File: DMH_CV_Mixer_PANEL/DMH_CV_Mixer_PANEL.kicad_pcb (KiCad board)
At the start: 2 copper layers, 50 x 200 mm, 25 parts, among them J0 Panel_GND_Solder_Wire_Pad

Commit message: Panel design done
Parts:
- H10: value CV C Amt -> In C2
- H12: value Offset B -> In B1; footprint SynthStuff:Pot_Cutout_Tiny -> SynthStuff:Pot_Cutout_Tiny_attv_P110KH1
- H13: value CV B Amt -> In B2
- H14: value In C -> In C1
- H15: value In B -> In B1
- H17: value CV B -> In B2
- H18: value CV C -> In C2
- H19: value Offset D -> In D1; footprint SynthStuff:Pot_Cutout_Tiny -> SynthStuff:Pot_Cutout_Tiny_attv_P110KH1
- H20: value CV D Amt -> In D2
- H21: value In D -> In D1
- H22: value CV D -> In D2
- H5: value Offset A -> In A1; footprint SynthStuff:Pot_Cutout_Tiny -> SynthStuff:Pot_Cutout_Tiny_attv_P110KH1
- H6: value CV A Amt -> In A2
- H7: value Offset C -> In C1; footprint SynthStuff:Pot_Cutout_Tiny -> SynthStuff:Pot_Cutout_Tiny_attv_P110KH1
- H8: value In A -> In A1
- H9: value CV A -> In A2
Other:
- board text added: "074-5"
- board text added: "MIXER"
- board text removed: "074-4"
- board text removed: "VCA"

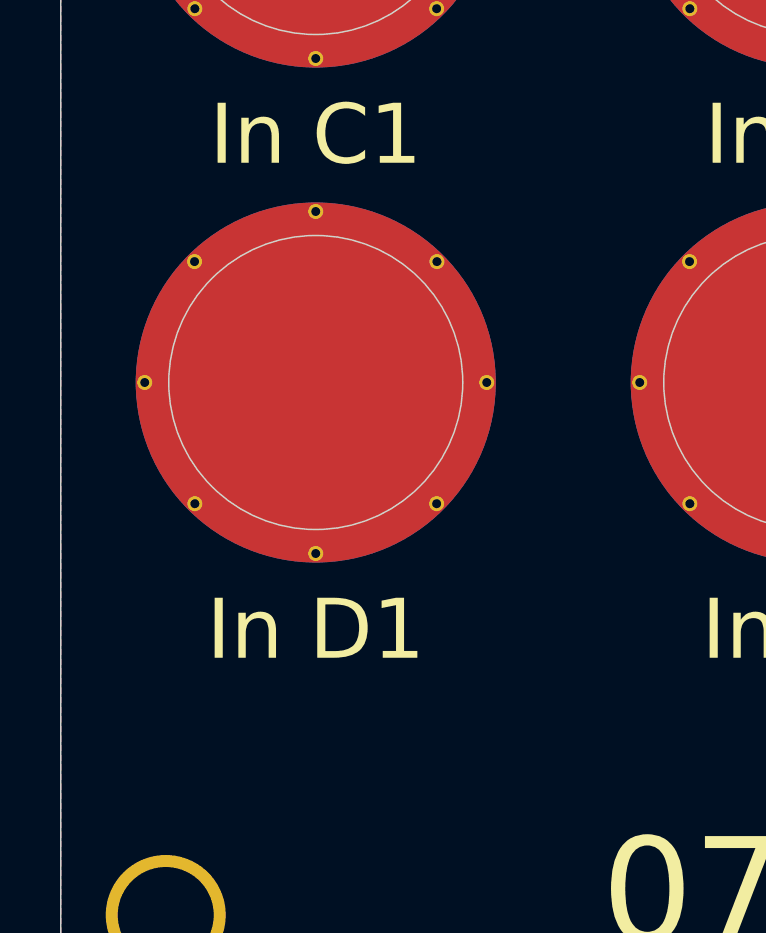
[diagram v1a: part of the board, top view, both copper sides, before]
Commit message: Finished IO page
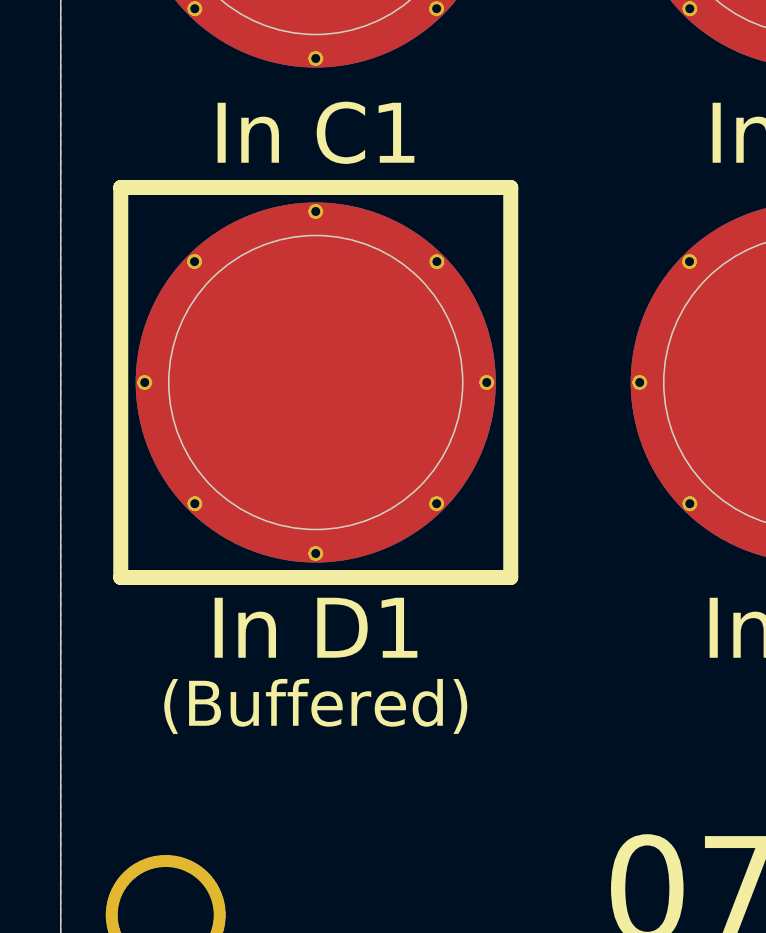
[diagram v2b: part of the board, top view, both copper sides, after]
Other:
- board text added: "(Buffered)"
